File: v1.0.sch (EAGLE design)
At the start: 174 parts, among them J1 DC-044-A, J2 MICROSD-9P, J3 2p-2.54, J4 2p-2.54, J5 16p-2.54, J6 16p-2.54, Q1 SI4532ADY, Q3 6pF@32.7680kHz, SW1 SW-200D, SW2 SW-200D, U1 MCP23017-E/SO, U10 74HC139N, U11 BZX84C30, U2 MCP79412-I/SN, U3 LOPY, U4 GROVE_DC&DC, U5 LM1085IT-5.0, U6 FT232RL-SSOP28, U7 2x14p-2.54, U8 FT232RL-SSOP28, U9 SP483ECN-L, X1 JST-XH-05-PIN-ROUND-PAD, X10 JST-XH-07-PIN-ROUND-PAD, X11 JST-XH-07-PIN-ROUND-PAD, X12 JST-XH-07-PIN-ROUND-PAD, X13 JST-XH-05-PIN-ROUND-PAD, X14 JST-XH-05-PIN-ROUND-PAD, X15 JST-XH-05-PIN-ROUND-PAD, X16 JST-XH-05-PIN-ROUND-PAD, X17 JST-XH-05-PIN-ROUND-PAD, X18 JST-XH-05-PIN-ROUND-PAD, X19 JST-XH-05-PIN-ROUND-PAD, X2 JST-XH-05-PIN-ROUND-PAD, X20 JST-XH-05-PIN-ROUND-PAD, X21 JST-XH-05-PIN-ROUND-PAD, X22 JST-XH-07-PIN-ROUND-PAD, X23 JST-XH-05-PIN-ROUND-PAD, X24 JST-XH-07-PIN-ROUND-PAD, X25 JST-XH-07-PIN-ROUND-PAD, X26 JST-XH-05-PIN-ROUND-PAD, X27 JST-XH-07-PIN-ROUND-PAD, X28 JST-XH-05-PIN-ROUND-PAD, X3 JST-XH-05-PIN-ROUND-PAD, X4 JST-XH-07-PIN-ROUND-PAD, X5 JST-XH-07-PIN-ROUND-PAD, X6 JST-XH-07-PIN-ROUND-PAD, X7 JST-XH-07-PIN-ROUND-PAD, X8 JST-XH-07-PIN-ROUND-PAD, X9 JST-XH-07-PIN-ROUND-PAD

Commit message: finally thyristor - to check the library and grid
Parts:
- added U$3: MCR703A, MCR703A:MCR703A
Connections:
- new net N$77: U$3.C
- new net N$78: U$3.A
- new net N$79: U$3.G
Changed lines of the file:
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@@
 <setting verticaltext="up"/>
 </settings>
-<grid distance="0.05" unitdist="inch" unit="inch" style="lines" multiple="1" display="no" altdistance="0.01" altunitdist="inch" altunit="inch"/>
+<grid distance="0.05" unitdist="mm" unit="mm" style="lines" multiple="1" display="no" altdistance="0.005" altunitdist="inch" altunit="mm"/>
 <layers>
 <layer number="1" name="Top" color="4" fill="1" visible="no" active="no"/>
@@
 <part name="J5" library="Seeed-Connector" library_urn="urn:adsk.eagle:library:465" deviceset="DIP-BLACK-MALE-HEADER-VERT(16P-2.54)" device="" value="16p-2.54"/>
 <part name="J6" library="Seeed-Connector" library_urn="urn:adsk.eagle:library:465" deviceset="DIP-BLACK-MALE-HEADER-VERT(16P-2.54)" device="" value="16p-2.54"/>
+<part name="U$3" library="MCR703A" deviceset="MCR703A" device=""/>
 </parts>
 <sheets>
@@
 <instance part="R20" gate="G$1" x="50.8" y="180.34" rot="R90"/>
 <instance part="GND40" gate="1" x="60.96" y="163.83"/>
+<instance part="U$3" gate="G$1" x="79.93" y="215.9"/>
 </instances>
 <busses>
@@
 </segment>
 </net>
+<net name="N$77" class="0">
+<segment>
+<pinref part="U$3" gate="G$1" pin="C"/>
+<wire x1="79.85" y1="212.1" x2="80.03" y2="212.1" width="0.1524" layer="91"/>
+<wire x1="80.03" y1="212.1" x2="79.93" y2="213.36" width="0.1524" layer="91"/>
+</segment>
+</net>
+<net name="N$78" class="0">
+<segment>
+<pinref part="U$3" gate="G$1" pin="A"/>
+<wire x1="79.93" y1="218.44" x2="80" y2="218.89" width="0.1524" layer="91"/>
+<wire x1="80" y1="218.89" x2="80" y2="220.6" width="0.1524" layer="91"/>
+</segment>
+</net>
+<net name="N$79" class="0">
+<segment>
+<pinref part="U$3" gate="G$1" pin="G"/>
+<wire x1="77.39" y1="213.36" x2="60.9" y2="213.26" width="0.1524" layer="91"/>
+<wire x1="60.9" y1="213.26" x2="61" y2="187.9" width="0.1524" layer="91"/>
+</segment>
+</net>

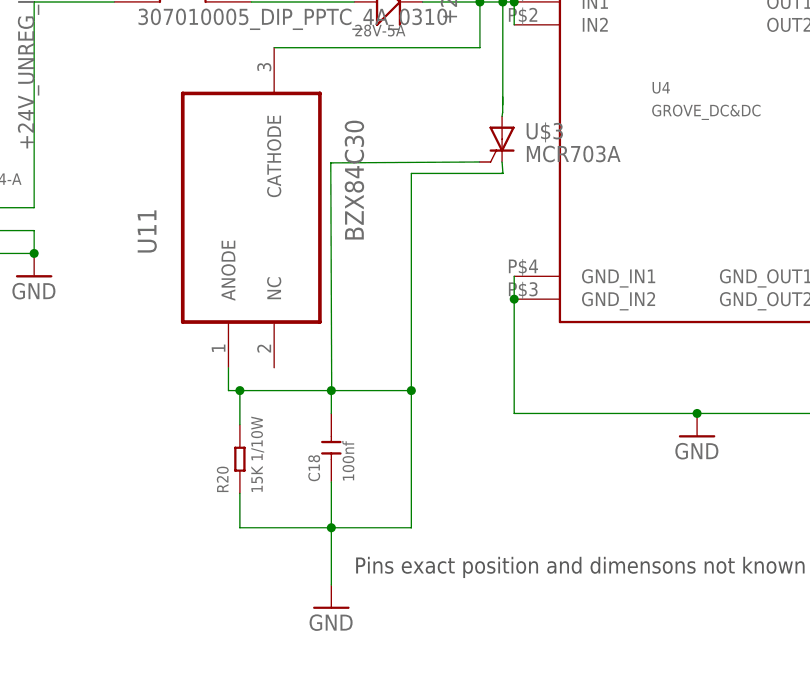
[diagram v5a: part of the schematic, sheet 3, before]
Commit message: changing ldo
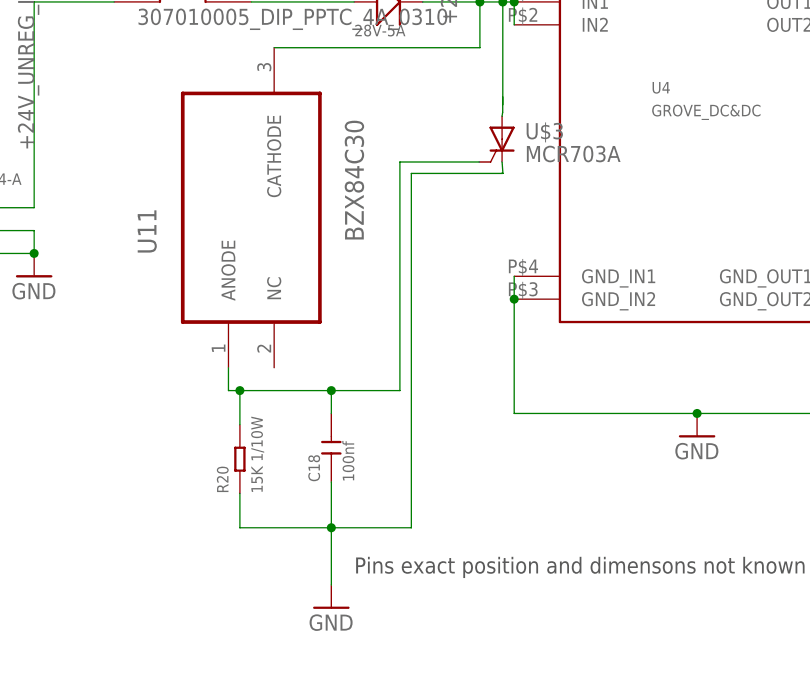
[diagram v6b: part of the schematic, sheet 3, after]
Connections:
- removed net N$79: U$3.G
- new net N$80: C18.2, R20.2, U$3.G, U11.ANODE
- net GND: no longer C18.2, R20.2, U11.ANODE
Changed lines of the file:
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@@
 <setting verticaltext="up"/>
 </settings>
-<grid distance="0.05" unitdist="mm" unit="mm" style="lines" multiple="1" display="no" altdistance="0.005" altunitdist="inch" altunit="mm"/>
+<grid distance="0.1" unitdist="inch" unit="inch" style="lines" multiple="1" display="no" altdistance="0.01" altunitdist="inch" altunit="inch"/>
 <layers>
 <layer number="1" name="Top" color="4" fill="1" visible="no" active="no"/>
@@
 <segment>
 <wire x1="80.01" y1="212.09" x2="69.85" y2="212.09" width="0.1524" layer="91"/>
-<wire x1="69.85" y1="212.09" x2="69.85" y2="187.96" width="0.1524" layer="91"/>
-<wire x1="69.85" y1="187.96" x2="60.96" y2="187.96" width="0.1524" layer="91"/>
-<wire x1="60.96" y1="187.96" x2="50.8" y2="187.96" width="0.1524" layer="91"/>
-<wire x1="69.85" y1="187.96" x2="69.85" y2="172.72" width="0.1524" layer="91"/>
-<junction x="69.85" y="187.96"/>
-<pinref part="C18" gate="G$1" pin="2"/>
-<wire x1="60.96" y1="187.96" x2="60.96" y2="185.42" width="0.1524" layer="91"/>
-<junction x="60.96" y="187.96"/>
+<wire x1="69.85" y1="212.09" x2="69.85" y2="172.72" width="0.1524" layer="91"/>
 <pinref part="R20" gate="G$1" pin="1"/>
 <wire x1="50.8" y1="176.53" x2="50.8" y2="172.72" width="0.1524" layer="91"/>
@@
 <wire x1="60.96" y1="172.72" x2="60.96" y2="166.37" width="0.1524" layer="91"/>
 <pinref part="GND40" gate="1" pin="GND"/>
-<pinref part="R20" gate="G$1" pin="2"/>
-<wire x1="50.8" y1="184.15" x2="50.8" y2="187.96" width="0.1524" layer="91"/>
-<pinref part="U11" gate="A" pin="ANODE"/>
-<wire x1="49.53" y1="190.5" x2="49.53" y2="187.96" width="0.1524" layer="91"/>
-<wire x1="49.53" y1="187.96" x2="50.8" y2="187.96" width="0.1524" layer="91"/>
-<junction x="50.8" y="187.96"/>
 </segment>
 <segment>
@@
 </segment>
 </net>
-<net name="N$79" class="0">
-<segment>
+<net name="N$80" class="0">
+<segment>
+<pinref part="C18" gate="G$1" pin="2"/>
+<wire x1="60.96" y1="187.96" x2="60.96" y2="185.42" width="0.1524" layer="91"/>
+<wire x1="60.96" y1="187.96" x2="50.8" y2="187.96" width="0.1524" layer="91"/>
+<pinref part="U11" gate="A" pin="ANODE"/>
+<wire x1="49.53" y1="190.5" x2="49.53" y2="187.96" width="0.1524" layer="91"/>
+<wire x1="49.53" y1="187.96" x2="50.8" y2="187.96" width="0.1524" layer="91"/>
+<junction x="50.8" y="187.96"/>
+<pinref part="R20" gate="G$1" pin="2"/>
+<wire x1="50.8" y1="184.15" x2="50.8" y2="187.96" width="0.1524" layer="91"/>
+<wire x1="60.96" y1="187.96" x2="68.58" y2="187.96" width="0.1524" layer="91"/>
+<wire x1="68.58" y1="187.96" x2="68.58" y2="213.36" width="0.1524" layer="91"/>
+<junction x="60.96" y="187.96"/>
 <pinref part="U$3" gate="G$1" pin="G"/>
-<wire x1="77.39" y1="213.36" x2="60.9" y2="213.26" width="0.1524" layer="91"/>
-<wire x1="60.9" y1="213.26" x2="61" y2="187.9" width="0.1524" layer="91"/>
-</segment>
-</net>
+<wire x1="77.39" y1="213.36" x2="68.58" y2="213.36" width="0.1524" layer="91"/>
+</segment>
+</net>

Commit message: corrections in
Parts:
- removed U5: LM1085IT-5.0, imported-parts:LM1085IT-5.0
- added U$4: MCR29300, mic29300:MCR29300
- U$3: value MCR703A -> C106DG; device MCR703A:MCR703A -> C106DG_thyristor:C106DG
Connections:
- removed net 6V5: C4.2, R7.2, TP4.TP, U4.OUT1, U4.OUT2, U5.VIN
- removed net N$77: U$3.C
- removed net N$78: U$3.A
- new net 5V35: C4.2, R7.2, TP4.TP, U$4.VIN, U4.OUT1, U4.OUT2
- net +24V: now also U$3.A
- net +3V3: now also PCB1.3V3@17
- net +5V: now also U$4.VOUT; no longer U5.VOUT
- net GND: now also U$3.C, U$4.ADJ/GND; no longer U5.ADJ/GND
- net N$80: now also U$3.G1; no longer U$3.G
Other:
- note added: "RPI has 1.8K pull up resistors for i2c"
- note added: "Seeed does not have sockets between 16 and 40 pins"
- note added: "my library"
- moved on the sheet: U$3
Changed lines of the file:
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@@
 <part name="X3" library="Rembrandt Electronics - JST XH Connectors v1-0 2" deviceset="JST-XH-05-PIN" device="-ROUND-PAD"/>
 <part name="FRAME6" library="frames" library_urn="urn:adsk.eagle:library:229" deviceset="A3L-LOC" device=""/>
-<part name="U5" library="imported-parts" deviceset="LM1085IT-5.0" device=""/>
 <part name="C4" library="Seeed-Capacitor" library_urn="urn:adsk.eagle:library:464" deviceset="CERAMIC-10UF-10V-10%-X5R(0603)" device="" value="10uf"/>
 <part name="GND27" library="supply1" library_urn="urn:adsk.eagle:library:371" deviceset="GND" device=""/>
@@
 <part name="J5" library="Seeed-Connector" library_urn="urn:adsk.eagle:library:465" deviceset="DIP-BLACK-MALE-HEADER-VERT(16P-2.54)" device="" value="16p-2.54"/>
 <part name="J6" library="Seeed-Connector" library_urn="urn:adsk.eagle:library:465" deviceset="DIP-BLACK-MALE-HEADER-VERT(16P-2.54)" device="" value="16p-2.54"/>
-<part name="U$3" library="MCR703A" deviceset="MCR703A" device=""/>
+<part name="U$3" library="C106DG_thyristor" deviceset="C106DG" device=""/>
+<part name="U$4" library="mic29300" deviceset="MCR29300" device=""/>
 </parts>
 <sheets>
@@
 <text x="231.14" y="7.62" size="1.778" layer="97">Seed crystals have the wrong capacitance</text>
 <text x="187.96" y="27.94" size="1.778" layer="97">These need testing experiementally</text>
+<text x="170.18" y="243.84" size="1.778" layer="97">Seeed does not have sockets between 16 and 40 pins</text>
+<text x="327.66" y="205.74" size="1.778" layer="97">RPI has 1.8K pull up resistors for i2c</text>
 </plain>
 <instances>
@@
 <pinref part="PCB1" gate="G$1" pin="3V3@1"/>
 <wire x1="71.12" y1="231.14" x2="91.44" y2="231.14" width="0.1524" layer="91"/>
+<pinref part="PCB1" gate="G$1" pin="3V3@17"/>
+<wire x1="91.44" y1="190.5" x2="91.44" y2="231.14" width="0.1524" layer="91"/>
+<junction x="91.44" y="231.14"/>
 </segment>
 <segment>
@@
 <wire x1="330.2" y1="193.04" x2="330.2" y2="256.54" width="0.1524" layer="97"/>
 <wire x1="330.2" y1="256.54" x2="331.47" y2="256.54" width="0.1524" layer="97"/>
+<text x="74.93" y="209.55" size="1.778" layer="97">my library</text>
 </plain>
 <instances>
@@
 <instance part="TP4" gate="G$1" x="129.54" y="233.68"/>
 <instance part="GND12" gate="1" x="27.94" y="200.66"/>
-<instance part="U5" gate="A" x="86.36" y="104.14"/>
 <instance part="C4" gate="G$1" x="53.34" y="96.52" rot="R90"/>
 <instance part="GND27" gate="1" x="53.34" y="60.96"/>
@@
 <instance part="R20" gate="G$1" x="50.8" y="180.34" rot="R90"/>
 <instance part="GND40" gate="1" x="60.96" y="163.83"/>
-<instance part="U$3" gate="G$1" x="79.93" y="215.9"/>
+<instance part="U$3" gate="G$1" x="81.28" y="215.9"/>
+<instance part="U$4" gate="G$1" x="86.36" y="99.06"/>
 </instances>
 <busses>
@@
 <wire x1="53.34" y1="92.71" x2="53.34" y2="86.36" width="0.1524" layer="91"/>
 <pinref part="GND27" gate="1" pin="GND"/>
-<pinref part="U5" gate="A" pin="ADJ/GND"/>
 <wire x1="53.34" y1="86.36" x2="53.34" y2="63.5" width="0.1524" layer="91"/>
 <wire x1="66.04" y1="99.06" x2="58.42" y2="99.06" width="0.1524" layer="91"/>
@@
 <wire x1="58.42" y1="86.36" x2="58.42" y2="99.06" width="0.1524" layer="91"/>
 <junction x="53.34" y="86.36"/>
+<pinref part="U$4" gate="G$1" pin="ADJ/GND"/>
 </segment>
 <segment>
@@
 </segment>
 <segment>
-<wire x1="80.01" y1="212.09" x2="69.85" y2="212.09" width="0.1524" layer="91"/>
+<wire x1="81.28" y1="212.09" x2="69.85" y2="212.09" width="0.1524" layer="91"/>
 <wire x1="69.85" y1="212.09" x2="69.85" y2="172.72" width="0.1524" layer="91"/>
 <pinref part="R20" gate="G$1" pin="1"/>
@@
 <wire x1="60.96" y1="172.72" x2="60.96" y2="166.37" width="0.1524" layer="91"/>
 <pinref part="GND40" gate="1" pin="GND"/>
+<pinref part="U$3" gate="G$1" pin="C"/>
+<wire x1="81.28" y1="213.36" x2="81.28" y2="212.09" width="0.1524" layer="91"/>
 </segment>
 <segment>
@@
 <junction x="81.28" y="231.14"/>
 <wire x1="77.47" y1="231.14" x2="77.47" y2="226.06" width="0.1524" layer="91"/>
-<wire x1="80.01" y1="231.14" x2="80.01" y2="219.71" width="0.1524" layer="91"/>
+<wire x1="80.01" y1="231.14" x2="80.01" y2="218.44" width="0.1524" layer="91"/>
 <junction x="80.01" y="231.14"/>
 <pinref part="U11" gate="A" pin="CATHODE"/>
 <wire x1="54.61" y1="226.06" x2="77.47" y2="226.06" width="0.1524" layer="91"/>
+<pinref part="U$3" gate="G$1" pin="A"/>
+<wire x1="81.28" y1="218.44" x2="80.01" y2="218.44" width="0.1524" layer="91"/>
 </segment>
 </net>
@@
 </segment>
 </net>
-<net name="6V5" class="0">
+<net name="5V35" class="0">
 <segment>
 <pinref part="U4" gate="G$1" pin="OUT1"/>
@@
 </segment>
 <segment>
-<pinref part="U5" gate="A" pin="VIN"/>
 <label x="48.26" y="101.6" size="1.778" layer="95"/>
 <wire x1="66.04" y1="101.6" x2="53.34" y2="101.6" width="0.1524" layer="91"/>
@@
 <wire x1="53.34" y1="100.33" x2="53.34" y2="101.6" width="0.1524" layer="91"/>
 <junction x="53.34" y="101.6"/>
+<pinref part="U$4" gate="G$1" pin="VIN"/>
 </segment>
 </net>
 <net name="+5V" class="0">
 <segment>
-<pinref part="U5" gate="A" pin="VOUT"/>
 <wire x1="106.68" y1="99.06" x2="111.76" y2="99.06" width="0.1524" layer="91"/>
 <pinref part="P+3" gate="1" pin="+5V"/>
@@
 <pinref part="TP1" gate="G$1" pin="TP"/>
 <junction x="111.76" y="99.06"/>
+<pinref part="U$4" gate="G$1" pin="VOUT"/>
 </segment>
 <segment>
@@
 </segment>
 </net>
-<net name="N$77" class="0">
-<segment>
-<pinref part="U$3" gate="G$1" pin="C"/>
-<wire x1="79.85" y1="212.1" x2="80.03" y2="212.1" width="0.1524" layer="91"/>
-<wire x1="80.03" y1="212.1" x2="79.93" y2="213.36" width="0.1524" layer="91"/>
-</segment>
-</net>
 <net name="N$78" class="0">
 <segment>
-<pinref part="U$3" gate="G$1" pin="A"/>
-<wire x1="79.93" y1="218.44" x2="80" y2="218.89" width="0.1524" layer="91"/>
 <wire x1="80" y1="218.89" x2="80" y2="220.6" width="0.1524" layer="91"/>
 </segment>
@@
 <wire x1="68.58" y1="187.96" x2="68.58" y2="213.36" width="0.1524" layer="91"/>
 <junction x="60.96" y="187.96"/>
-<pinref part="U$3" gate="G$1" pin="G"/>
-<wire x1="77.39" y1="213.36" x2="68.58" y2="213.36" width="0.1524" layer="91"/>
+<pinref part="U$3" gate="G$1" pin="G1"/>
+<wire x1="78.74" y1="213.36" x2="68.58" y2="213.36" width="0.1524" layer="91"/>
 </segment>
 </net>
@@
 </segment>
 </net>
-<net name="6V5" class="0">
+<net name="5V35" class="0">
 <segment>
 <pinref part="R7" gate="G$1" pin="2"/>

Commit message: corrections
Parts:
- removed D7: RED-0603, Seeed-LED-2016:LED-SMD-RED-DIFFUSED(0603)
- removed R8: 1K, Seeed-Resistor-2016:SMD-RES-1K-1%-1/10W(0603)
- added D10, D13, D14: RED-0603, Seeed-LED-2016:LED-SMD-RED-DIFFUSED(0603)
- added R11: 1K, Seeed-Resistor-2016:SMD-RES-1K-1%-1/10W(0603)
- added R21: 220R, Seeed-Resistor:DIP-RES-220R-5%-1/4W(PR-D2.3XL6.5MM)
- added R22: 100R, Seeed-Resistor:DIP-RES-100R-5%-1/4W(PR-D2.3XL6.5MM)
- added SW3, SW4: SW-200D, Seeed-Switch:DIP-TILT-SWITCH-SW-200D(2P-12X3.6MM)
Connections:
- removed net LOPY_P13: U3.P13, U7.25, U7.4
- removed net N$23: D4.-, D5.-, D6.-, D7.-, D8.-, D9.-, SW1.1
- removed net N$31: D7.+, R8.1
- new net N$77: D10.+, R11.1
- new net N$81: D4.-, D5.-, D6.-, SW1.1
- new net N$82: D14.+, R22.1
- new net N$83: D10.-, D14.-, SW4.1
- new net N$86: D13.-, D8.-, D9.-
- new net N$87: D13.+, R21.1
- new net N$89: SW3.1
- net GND: now also SW3.2, SW4.2
- net LOPY_3V3: now also R22.2, U7.25, U7.4
- net LOPY_USB_5V: now also R11.2; no longer R8.2
- net PI_5V: now also R21.2
- net PI_PWR_CTRL: now also U3.P13
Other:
- note added: "the only battery holder on seeed"
- moved on the sheet: SW1
